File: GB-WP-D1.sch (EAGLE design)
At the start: 10 parts

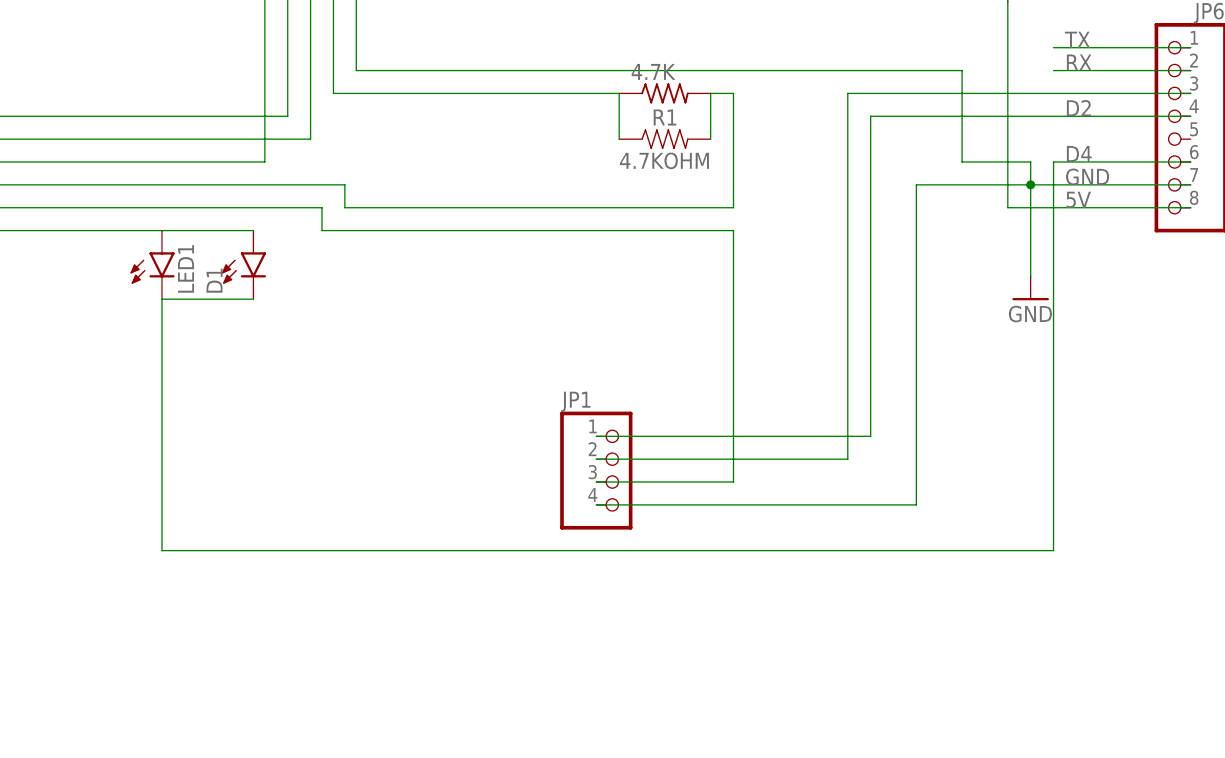
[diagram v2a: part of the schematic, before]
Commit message: Add files via upload
SMT Jumpers for the OLED's GND and VCC
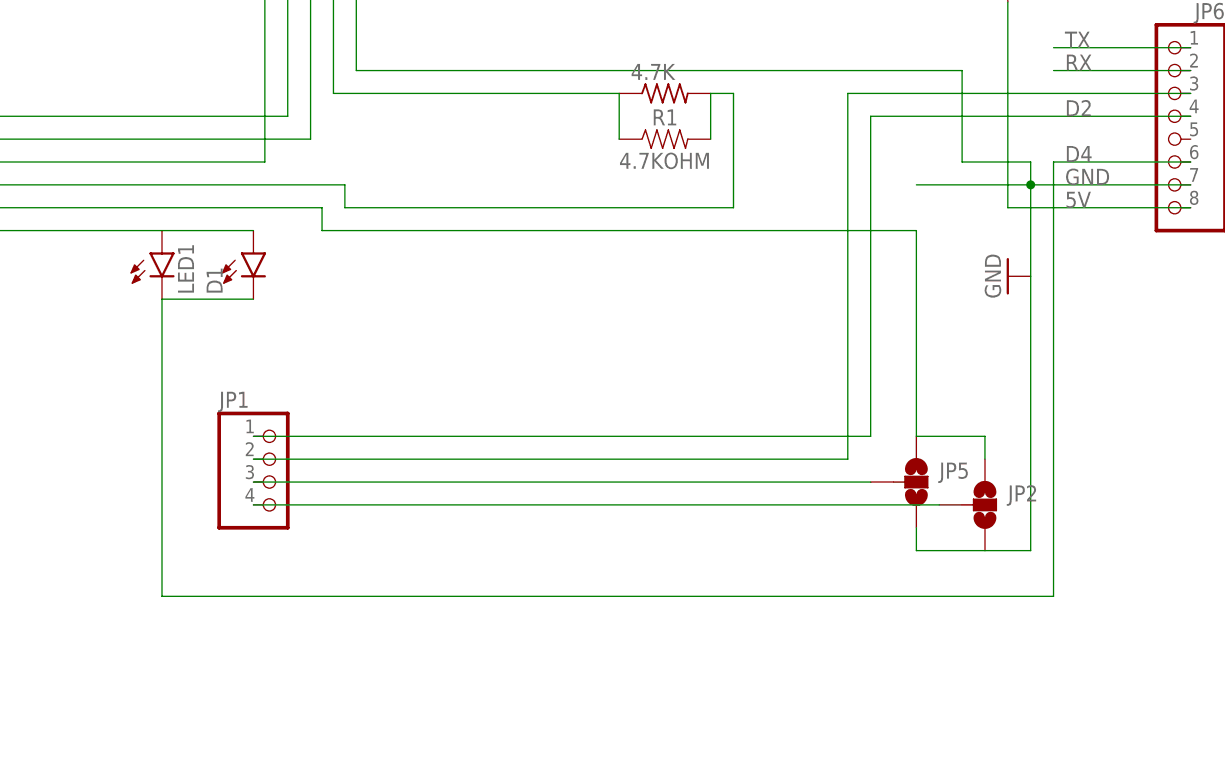
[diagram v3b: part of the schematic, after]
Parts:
- added JP2, JP5: JUMPER-SMT_3_NO_NO-SILK, SparkFun-Jumpers:JUMPER-SMT_3_NO_NO-SILK
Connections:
- new net N$2: JP1.3, JP5.2
- new net N$3: JP1.4, JP2.2
- net 3.3V: now also JP2.1, JP5.1; no longer JP1.3
- net GND: now also JP2.3, JP5.3; no longer JP1.4
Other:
- moved on the sheet: JP1
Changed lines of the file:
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@@
 <part name="D1" library="SparkFun-LED" deviceset="LED" device="1206"/>
 <part name="R1" library="SparkFun-Resistors" deviceset="4.7KOHM" device=""/>
+<part name="JP2" library="SparkFun-Jumpers" deviceset="JUMPER-SMT_3_NO" device="_NO-SILK"/>
+<part name="JP5" library="SparkFun-Jumpers" deviceset="JUMPER-SMT_3_NO" device="_NO-SILK"/>
 </parts>
 <sheets>
@@
 <attribute name="VALUE" x="52.324" y="120.396" size="1.778" layer="96"/>
 </instance>
-<instance part="GND1" gate="1" x="205.74" y="83.82" smashed="yes">
-<attribute name="VALUE" x="203.2" y="81.28" size="1.778" layer="96"/>
+<instance part="GND1" gate="1" x="203.2" y="86.36" smashed="yes" rot="R270">
+<attribute name="VALUE" x="200.66" y="88.9" size="1.778" layer="96" rot="R270"/>
 </instance>
 <instance part="4.7K" gate="G$1" x="165.1" y="106.68" smashed="yes">
@@
 <attribute name="VALUE" x="135.89" y="120.65" size="1.778" layer="96" rot="R90"/>
 </instance>
-<instance part="JP1" gate="A" x="160.02" y="63.5" smashed="yes">
-<attribute name="NAME" x="153.67" y="71.755" size="1.778" layer="95"/>
-<attribute name="VALUE" x="153.67" y="55.88" size="1.778" layer="96"/>
+<instance part="JP1" gate="A" x="121.92" y="63.5" smashed="yes">
+<attribute name="NAME" x="115.57" y="71.755" size="1.778" layer="95"/>
+<attribute name="VALUE" x="115.57" y="55.88" size="1.778" layer="96"/>
 </instance>
 <instance part="LED1" gate="G$1" x="109.22" y="88.9" smashed="yes">
@@
 <attribute name="NAME" x="165.1" y="103.124" size="1.778" layer="95" font="vector" align="bottom-center"/>
 <attribute name="VALUE" x="165.1" y="100.076" size="1.778" layer="96" font="vector" align="top-center"/>
+</instance>
+<instance part="JP2" gate="G$1" x="200.66" y="60.96" smashed="yes">
+<attribute name="NAME" x="203.2" y="61.341" size="1.778" layer="95" font="vector"/>
+</instance>
+<instance part="JP5" gate="G$1" x="193.04" y="63.5" smashed="yes">
+<attribute name="NAME" x="195.58" y="63.881" size="1.778" layer="95" font="vector"/>
 </instance>
 </instances>
@@
 <wire x1="205.74" y1="96.52" x2="193.04" y2="96.52" width="0.1524" layer="91"/>
 <junction x="205.74" y="96.52"/>
-<wire x1="193.04" y1="96.52" x2="193.04" y2="60.96" width="0.1524" layer="91"/>
-<wire x1="193.04" y1="60.96" x2="157.48" y2="60.96" width="0.1524" layer="91"/>
-<pinref part="JP1" gate="A" pin="4"/>
 <pinref part="U$2" gate="G$1" pin="GND"/>
 <pinref part="JP4" gate="A" pin="6"/>
@@
 <wire x1="205.74" y1="99.06" x2="205.74" y2="96.52" width="0.1524" layer="91"/>
 <pinref part="JP6" gate="A" pin="7"/>
+<pinref part="JP5" gate="G$1" pin="3"/>
+<pinref part="JP2" gate="G$1" pin="3"/>
+<wire x1="193.04" y1="58.42" x2="193.04" y2="55.88" width="0.1524" layer="91"/>
+<wire x1="193.04" y1="55.88" x2="200.66" y2="55.88" width="0.1524" layer="91"/>
+<wire x1="200.66" y1="55.88" x2="205.74" y2="55.88" width="0.1524" layer="91"/>
+<wire x1="205.74" y1="55.88" x2="205.74" y2="86.36" width="0.1524" layer="91"/>
 </segment>
 </net>
@@
 <wire x1="223.52" y1="104.14" x2="187.96" y2="104.14" width="0.1524" layer="91"/>
 <wire x1="187.96" y1="104.14" x2="187.96" y2="68.58" width="0.1524" layer="91"/>
-<wire x1="187.96" y1="68.58" x2="157.48" y2="68.58" width="0.1524" layer="91"/>
+<wire x1="187.96" y1="68.58" x2="119.38" y2="68.58" width="0.1524" layer="91"/>
 <pinref part="JP1" gate="A" pin="1"/>
 <pinref part="JP6" gate="A" pin="4"/>
@@
 <segment>
 <label x="209.55" y="99.06" size="1.778" layer="95"/>
-<wire x1="208.28" y1="99.06" x2="208.28" y2="55.88" width="0.1524" layer="91"/>
+<wire x1="208.28" y1="99.06" x2="208.28" y2="50.8" width="0.1524" layer="91"/>
 <pinref part="LED1" gate="G$1" pin="C"/>
-<wire x1="208.28" y1="55.88" x2="109.22" y2="55.88" width="0.1524" layer="91"/>
-<wire x1="109.22" y1="55.88" x2="109.22" y2="83.82" width="0.1524" layer="91"/>
+<wire x1="208.28" y1="50.8" x2="109.22" y2="50.8" width="0.1524" layer="91"/>
+<wire x1="109.22" y1="50.8" x2="109.22" y2="83.82" width="0.1524" layer="91"/>
 <pinref part="JP6" gate="A" pin="6"/>
 <wire x1="223.52" y1="99.06" x2="208.28" y2="99.06" width="0.1524" layer="91"/>
@@
 <wire x1="53.34" y1="93.98" x2="127" y2="93.98" width="0.1524" layer="91"/>
 <wire x1="127" y1="93.98" x2="127" y2="91.44" width="0.1524" layer="91"/>
-<wire x1="127" y1="91.44" x2="172.72" y2="91.44" width="0.1524" layer="91"/>
-<wire x1="172.72" y1="91.44" x2="172.72" y2="63.5" width="0.1524" layer="91"/>
-<pinref part="JP1" gate="A" pin="3"/>
-<wire x1="172.72" y1="63.5" x2="157.48" y2="63.5" width="0.1524" layer="91"/>
+<wire x1="127" y1="91.44" x2="193.04" y2="91.44" width="0.1524" layer="91"/>
 <wire x1="109.22" y1="91.44" x2="119.38" y2="91.44" width="0.1524" layer="91"/>
 <pinref part="D1" gate="D1" pin="A"/>
+<pinref part="JP5" gate="G$1" pin="1"/>
+<wire x1="193.04" y1="91.44" x2="193.04" y2="68.58" width="0.1524" layer="91"/>
+<pinref part="JP2" gate="G$1" pin="1"/>
+<wire x1="193.04" y1="68.58" x2="200.66" y2="68.58" width="0.1524" layer="91"/>
+<wire x1="200.66" y1="68.58" x2="200.66" y2="66.04" width="0.1524" layer="91"/>
 </segment>
 </net>
@@
 <wire x1="223.52" y1="106.68" x2="185.42" y2="106.68" width="0.1524" layer="91"/>
 <wire x1="185.42" y1="106.68" x2="185.42" y2="66.04" width="0.1524" layer="91"/>
-<wire x1="185.42" y1="66.04" x2="157.48" y2="66.04" width="0.1524" layer="91"/>
+<wire x1="185.42" y1="66.04" x2="119.38" y2="66.04" width="0.1524" layer="91"/>
 <pinref part="JP1" gate="A" pin="2"/>
 <pinref part="JP6" gate="A" pin="3"/>
 </segment>
 </net>
+<net name="N$2" class="0">
+<segment>
+<pinref part="JP1" gate="A" pin="3"/>
+<pinref part="JP5" gate="G$1" pin="2"/>
+<wire x1="119.38" y1="63.5" x2="187.96" y2="63.5" width="0.1524" layer="91"/>
+</segment>
+</net>
+<net name="N$3" class="0">
+<segment>
+<pinref part="JP2" gate="G$1" pin="2"/>
+<pinref part="JP1" gate="A" pin="4"/>
+<wire x1="195.58" y1="60.96" x2="119.38" y2="60.96" width="0.1524" layer="91"/>
+</segment>
+</net>

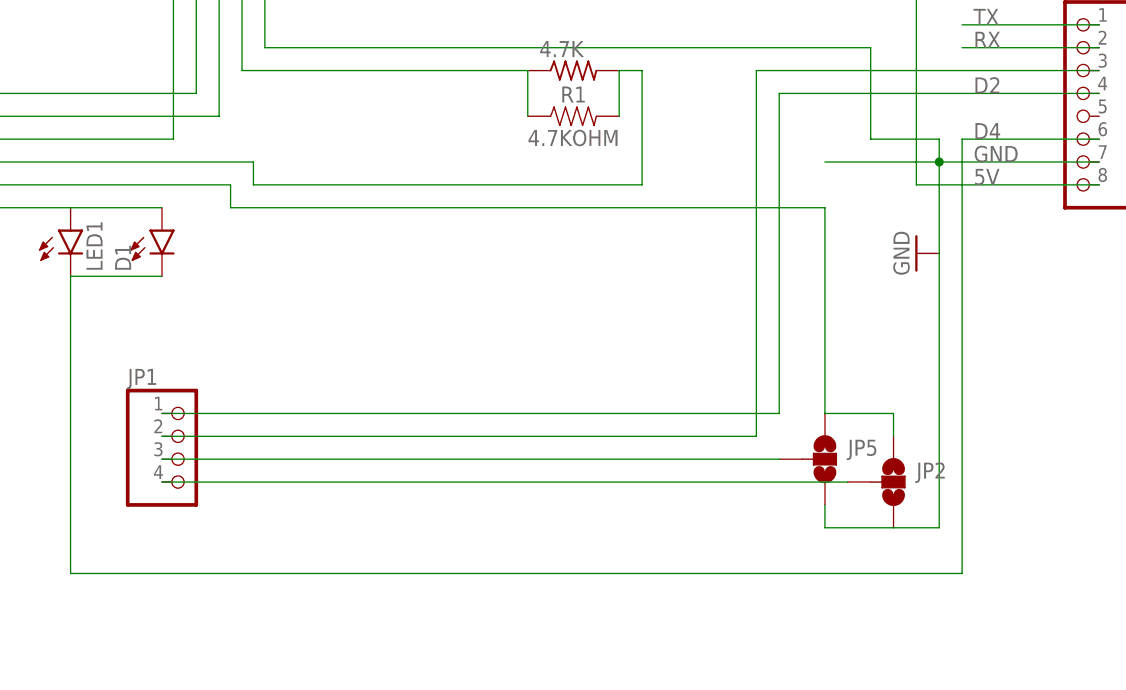
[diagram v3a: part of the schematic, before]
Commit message: Add files via upload
Unnecesari SMT Jumper config for OLED 128x32
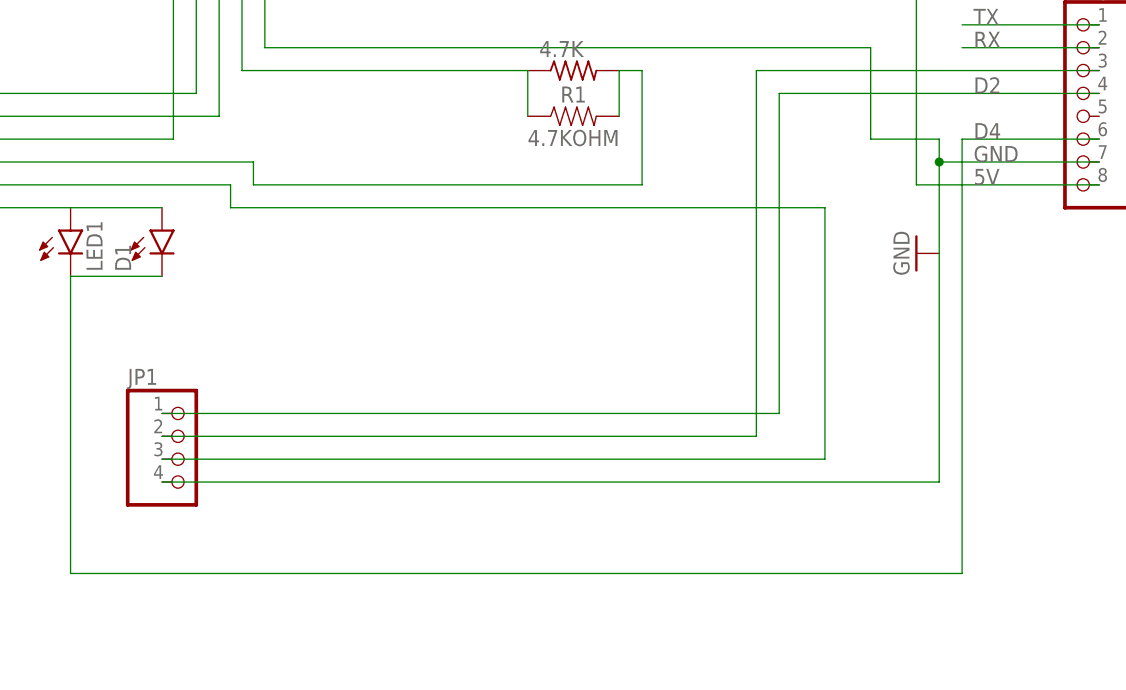
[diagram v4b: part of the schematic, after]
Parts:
- removed JP2, JP5: JUMPER-SMT_3_NO_NO-SILK, SparkFun-Jumpers:JUMPER-SMT_3_NO_NO-SILK
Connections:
- removed net N$2: JP1.3, JP5.2
- removed net N$3: JP1.4, JP2.2
- net 3.3V: now also JP1.3; no longer JP2.1, JP5.1
- net GND: now also JP1.4; no longer JP2.3, JP5.3
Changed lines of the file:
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@@
 <?xml version="1.0" encoding="utf-8"?>
 <!DOCTYPE eagle SYSTEM "eagle.dtd">
-<eagle version="9.6.2">
+<eagle version="9.6.1">
 <drawing>
 <settings>
@@
 <part name="D1" library="SparkFun-LED" deviceset="LED" device="1206"/>
 <part name="R1" library="SparkFun-Resistors" deviceset="4.7KOHM" device=""/>
-<part name="JP2" library="SparkFun-Jumpers" deviceset="JUMPER-SMT_3_NO" device="_NO-SILK"/>
-<part name="JP5" library="SparkFun-Jumpers" deviceset="JUMPER-SMT_3_NO" device="_NO-SILK"/>
 </parts>
 <sheets>
@@
 <attribute name="VALUE" x="165.1" y="100.076" size="1.778" layer="96" font="vector" align="top-center"/>
 </instance>
-<instance part="JP2" gate="G$1" x="200.66" y="60.96" smashed="yes">
-<attribute name="NAME" x="203.2" y="61.341" size="1.778" layer="95" font="vector"/>
-</instance>
-<instance part="JP5" gate="G$1" x="193.04" y="63.5" smashed="yes">
-<attribute name="NAME" x="195.58" y="63.881" size="1.778" layer="95" font="vector"/>
-</instance>
 </instances>
 <busses>
@@
 <pinref part="GND1" gate="1" pin="GND"/>
 <wire x1="205.74" y1="96.52" x2="205.74" y2="86.36" width="0.1524" layer="91"/>
-<wire x1="205.74" y1="96.52" x2="193.04" y2="96.52" width="0.1524" layer="91"/>
 <junction x="205.74" y="96.52"/>
 <pinref part="U$2" gate="G$1" pin="GND"/>
@@
 <wire x1="205.74" y1="99.06" x2="205.74" y2="96.52" width="0.1524" layer="91"/>
 <pinref part="JP6" gate="A" pin="7"/>
-<pinref part="JP5" gate="G$1" pin="3"/>
-<pinref part="JP2" gate="G$1" pin="3"/>
-<wire x1="193.04" y1="58.42" x2="193.04" y2="55.88" width="0.1524" layer="91"/>
-<wire x1="193.04" y1="55.88" x2="200.66" y2="55.88" width="0.1524" layer="91"/>
-<wire x1="200.66" y1="55.88" x2="205.74" y2="55.88" width="0.1524" layer="91"/>
-<wire x1="205.74" y1="55.88" x2="205.74" y2="86.36" width="0.1524" layer="91"/>
+<wire x1="205.74" y1="60.96" x2="205.74" y2="86.36" width="0.1524" layer="91"/>
+<pinref part="JP1" gate="A" pin="4"/>
+<wire x1="205.74" y1="60.96" x2="119.38" y2="60.96" width="0.1524" layer="91"/>
 </segment>
 </net>
@@
 <wire x1="109.22" y1="91.44" x2="119.38" y2="91.44" width="0.1524" layer="91"/>
 <pinref part="D1" gate="D1" pin="A"/>
-<pinref part="JP5" gate="G$1" pin="1"/>
-<wire x1="193.04" y1="91.44" x2="193.04" y2="68.58" width="0.1524" layer="91"/>
-<pinref part="JP2" gate="G$1" pin="1"/>
-<wire x1="193.04" y1="68.58" x2="200.66" y2="68.58" width="0.1524" layer="91"/>
-<wire x1="200.66" y1="68.58" x2="200.66" y2="66.04" width="0.1524" layer="91"/>
+<wire x1="193.04" y1="91.44" x2="193.04" y2="63.5" width="0.1524" layer="91"/>
+<pinref part="JP1" gate="A" pin="3"/>
+<wire x1="119.38" y1="63.5" x2="193.04" y2="63.5" width="0.1524" layer="91"/>
 </segment>
 </net>
@@
 </segment>
 </net>
-<net name="N$2" class="0">
-<segment>
-<pinref part="JP1" gate="A" pin="3"/>
-<pinref part="JP5" gate="G$1" pin="2"/>
-<wire x1="119.38" y1="63.5" x2="187.96" y2="63.5" width="0.1524" layer="91"/>
-</segment>
-</net>
-<net name="N$3" class="0">
-<segment>
-<pinref part="JP2" gate="G$1" pin="2"/>
-<pinref part="JP1" gate="A" pin="4"/>
-<wire x1="195.58" y1="60.96" x2="119.38" y2="60.96" width="0.1524" layer="91"/>
-</segment>
-</net>
